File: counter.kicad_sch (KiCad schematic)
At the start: 6 parts, among them U1 74LS193, U11 74LS193, U2 74LS193, U3 74LS193, U4 74LS193, U5 74LS193

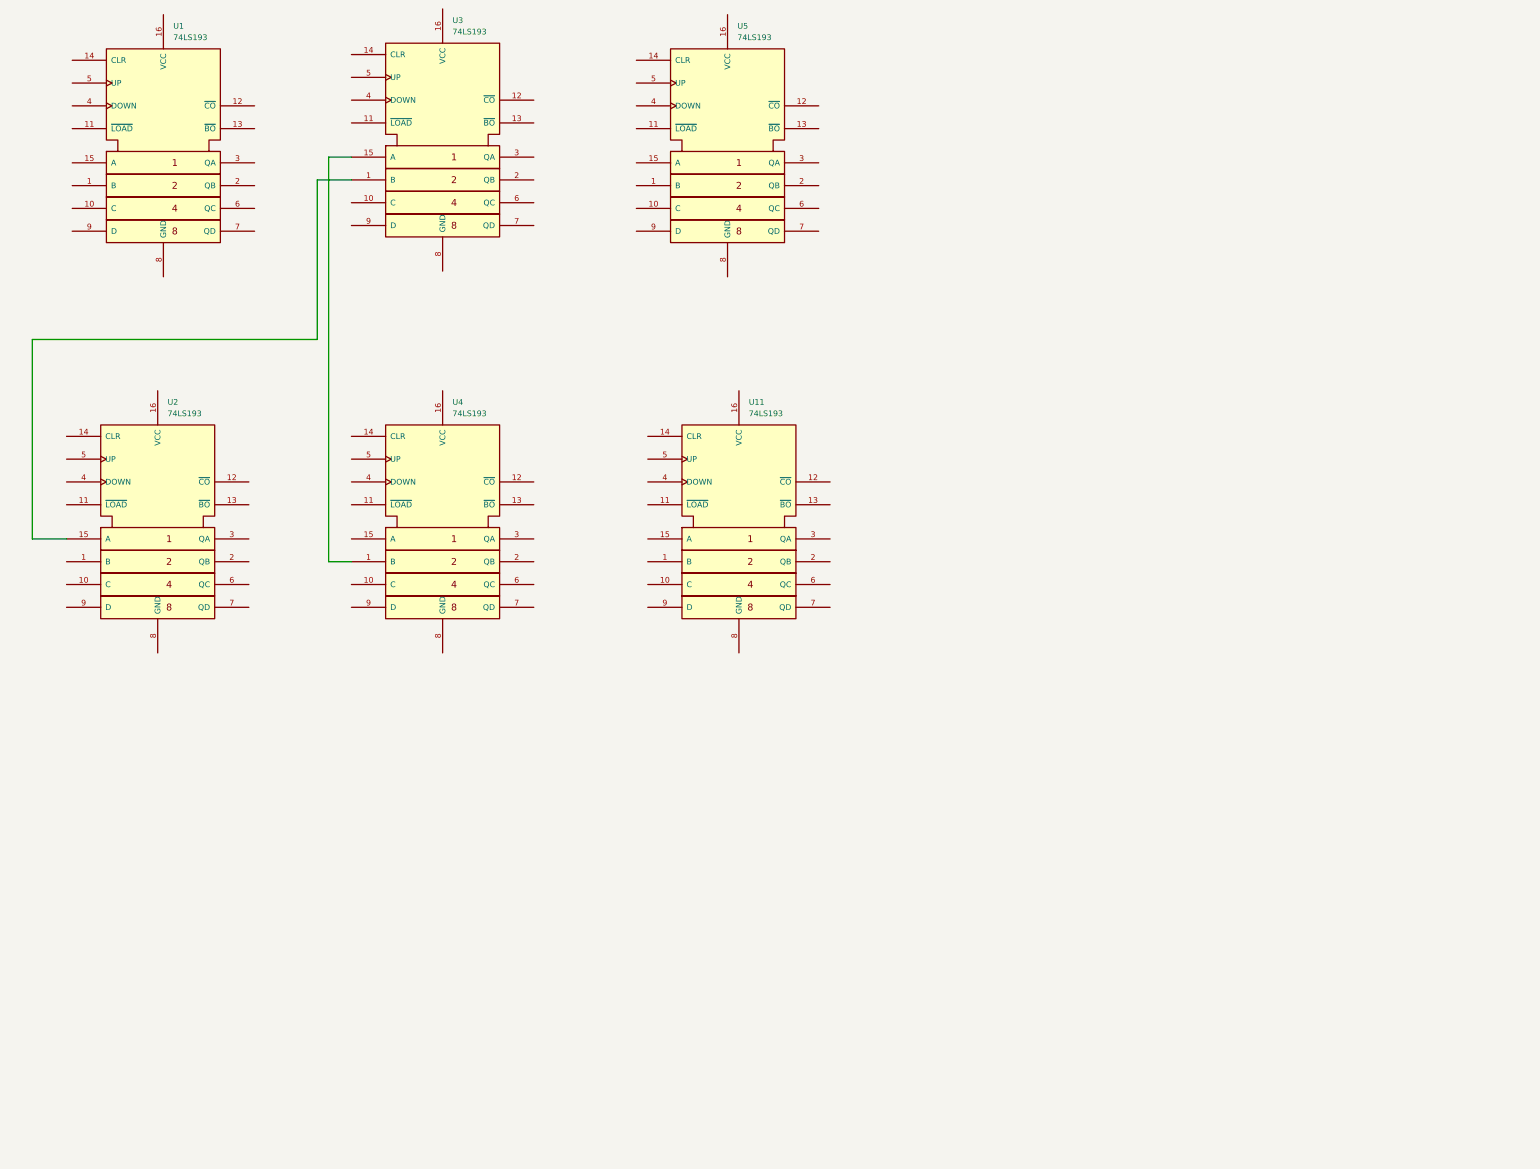
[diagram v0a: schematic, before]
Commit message: Einige Verbindungen im Bereich des Zählers ermittelt
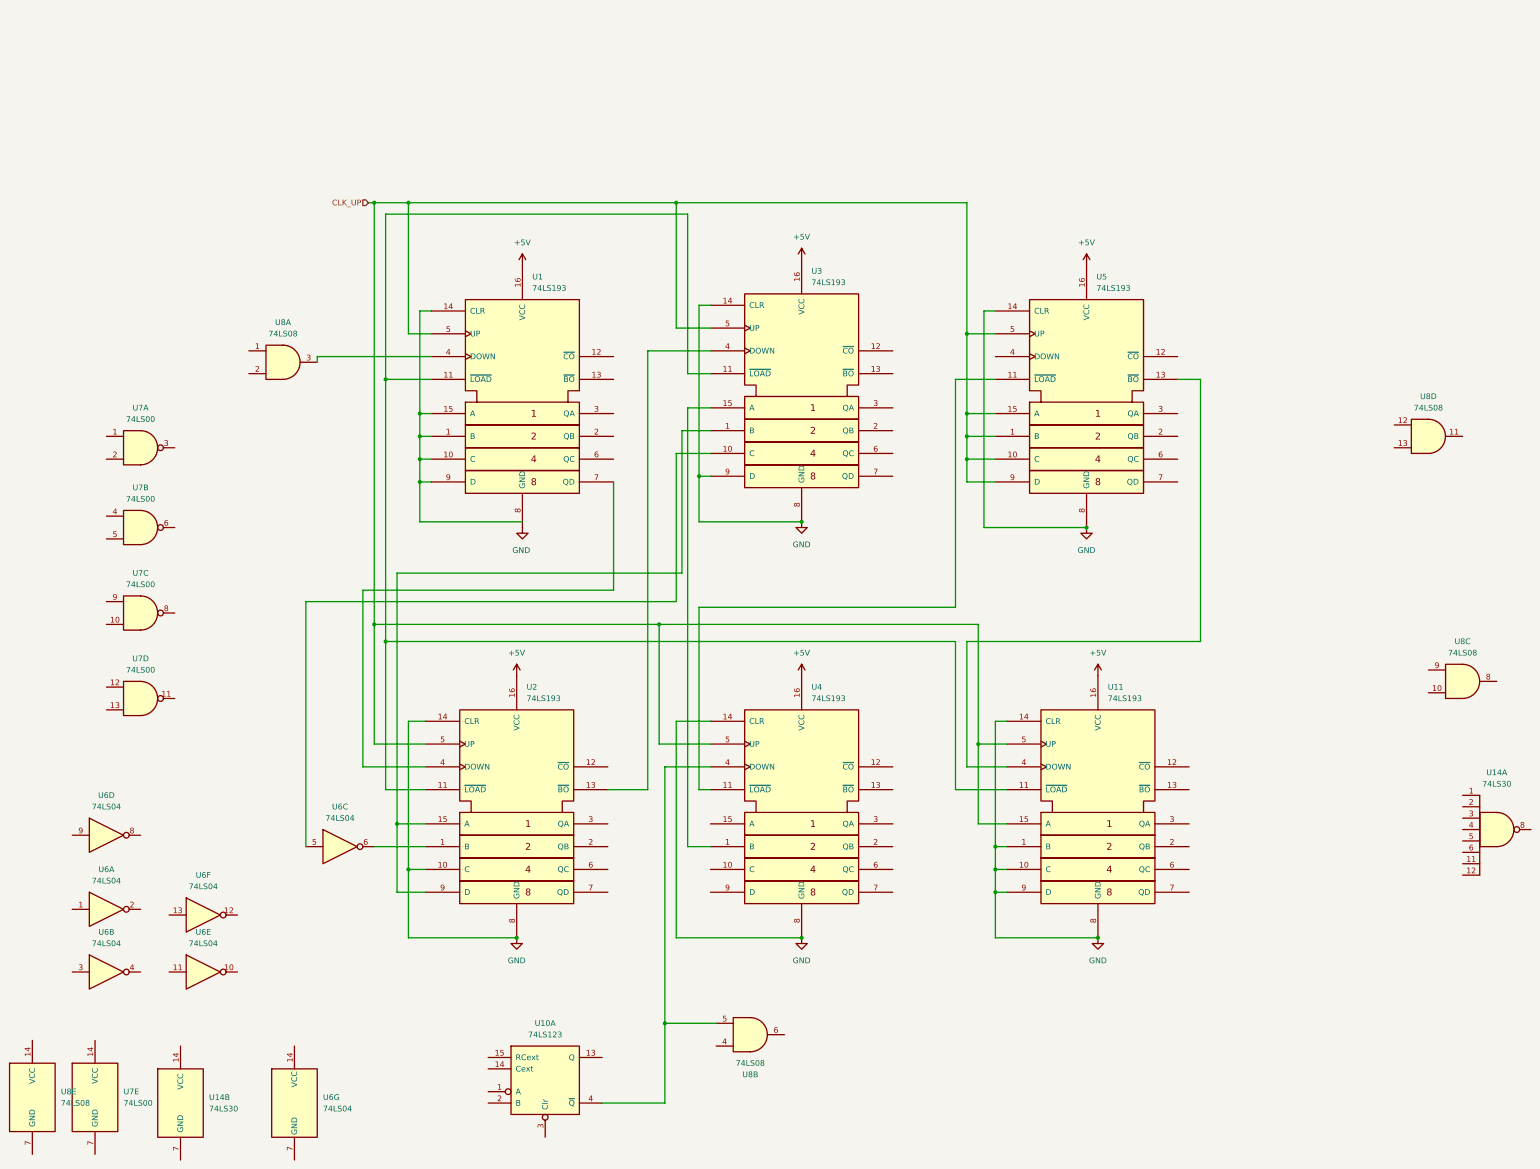
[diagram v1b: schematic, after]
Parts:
- added U10: 74LS123, Package_DIP:DIP-16_W7.62mm, symbol 74xx:74LS123
- added U14: 74LS30, Package_DIP:DIP-14_W7.62mm, symbol 74xx:74LS30
- added U6: 74LS04, Package_DIP:DIP-14_W7.62mm, symbol 74xx:74LS04
- added U7: 74LS00, Package_DIP:DIP-14_W7.62mm, symbol 74xx:74LS00
- added U8: 74LS08, Package_DIP:DIP-14_W7.62mm, symbol 74xx:74LS08
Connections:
- net at U1.1 (B): now also U1.10 (C), U1.14 (CLR), U1.15 (A), U1.9 (D)
- net at U1.11 (~{LOAD}): now also U11.11 (~{LOAD}), U2.11 (~{LOAD}), U3.11 (~{LOAD})
- net +5V: now reaches U1.16 (VCC)
- net +5V: now also U11.16 (VCC), U2.16 (VCC), U3.16 (VCC), U4.16 (VCC), U5.16 (VCC)
- net at U1.4 (DOWN): now also U8.3
- net CLK_UP: now reaches U1.5 (UP)
- net CLK_UP: now also U11.15 (A), U11.5 (UP), U2.5 (UP), U3.5 (UP), U4.5 (UP), U5.1 (B), U5.10 (C), U5.15 (A), U5.5 (UP), U5.9 (D)
- net at U1.7 (QD): now also U2.4 (DOWN)
- net GND: now reaches U1.8 (GND)
- net GND: now also U11.1 (B), U11.10 (C), U11.14 (CLR), U11.8 (GND), U11.9 (D), U2.10 (C), U2.14 (CLR), U2.8 (GND), U3.14 (CLR), U3.8 (GND), U3.9 (D), U4.14 (CLR), U4.8 (GND), U5.14 (CLR), U5.8 (GND)
- net at U5.11 (~{LOAD}): now also U4.11 (~{LOAD})
- net at U5.13 (~{BO}): now also U11.4 (DOWN)
- net at U2.15 (A), U3.1 (B): now also U2.9 (D)
- net at U3.10 (C): now also U6.5
- net at U3.4 (DOWN): now also U2.13 (~{BO})
- net at U4.4 (DOWN): now also U10.4 (~{Q}), U8.5
- net at U2.1 (B): now also U6.6
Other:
- moved on the sheet: U1, U11, U2, U3, U4, U5

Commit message: Aufnahme Schaltplan wip
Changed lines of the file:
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@@
+		)
+	)
+	(hierarchical_label "SRV_CLK_TTL"
+		(shape input)
+		(at 33.02 60.96 0)
+		(fields_autoplaced yes)
+		(effects
+			(font
+				(size 1.27 1.27)
+			)
+			(justify left)
 		)
 	)

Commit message: rev eng wip
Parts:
- added unit 2 of U10
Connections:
- net CLK_UP: now also U10.2 (B), U10.3 (Clr), U3.15 (A), U4.1 (B), U4.10 (C), U4.15 (A), U4.9 (D), U10.10 (B), U10.11 (Clr)
- net SRV_CLK_TTL: now also U14.2
- net UNIT_SELECT_TTL: now reaches U7.9
- net UNIT_SELECT_TTL: now also U3.10 (C), U6.5
- net LOAD_TTL______: now reaches U4.11 (~{LOAD}), U5.11 (~{LOAD})
- net at U5.13 (~{BO}): no longer U11.4 (DOWN)
- net U5_QA: now reaches U5.3 (QA)
- net at U5.4 (DOWN): now also U4.13 (~{BO})
- net at U2.15 (A), U2.9 (D), U3.1 (B): now also U2.1 (B), U6.6
- net at U3.13 (~{BO}): now also U11.4 (DOWN)
- net at U10.1 (A): now also U10.9 (A)
- net MonoflopA: now reaches U10.13 (Q)
- no-connect marks 0 -> 18
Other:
- moved on the sheet: U11

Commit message: Busses Names and more
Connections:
- net U5_QA renamed BIT10_TTL
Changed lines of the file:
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@@
 		)
 	)
-	(hierarchical_label "U5_QA"
+	(hierarchical_label "BIT10_TTL"
 		(shape output)
 		(at 290.83 110.49 0)

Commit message: weitere verdrahtungen nachvollzogen
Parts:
- added C8, C9: ?nF, Capacitor_THT:C_Disc_D3.0mm_W1.6mm_P2.50mm, symbol Device:C_Small
- added R22, R23: 5,1KΩ, Resistor_THT:R_Axial_DIN0207_L6.3mm_D2.5mm_P7.62mm_Horizontal, symbol Device:R
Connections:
- net +5V: now also R22.1, R23.1
- net at U10.6 (Cext): now also C8.2
- net at U10.7 (RCext): now also C8.1, R22.2
- net at U10.14 (Cext): now also C9.2
- net at U10.15 (RCext): now also C9.1, R23.2
